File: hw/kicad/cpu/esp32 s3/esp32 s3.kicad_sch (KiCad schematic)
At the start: 42 parts, among them J1 TOP, J2 BUTTOM, J3 USB_B_Micro, SW1 SW_Push, U1 ESP32-S3-WROOM-1-N16R2, U2 ICM-42688-P

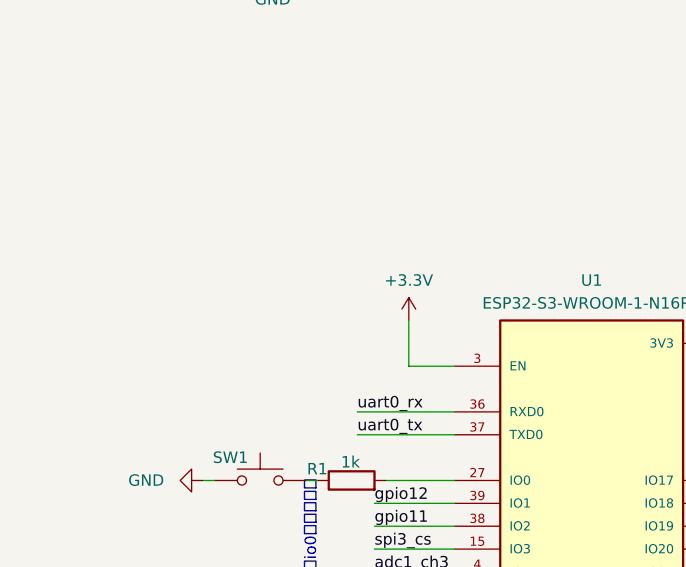
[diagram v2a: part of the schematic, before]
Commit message: 更新ESP32 S3 CPU板
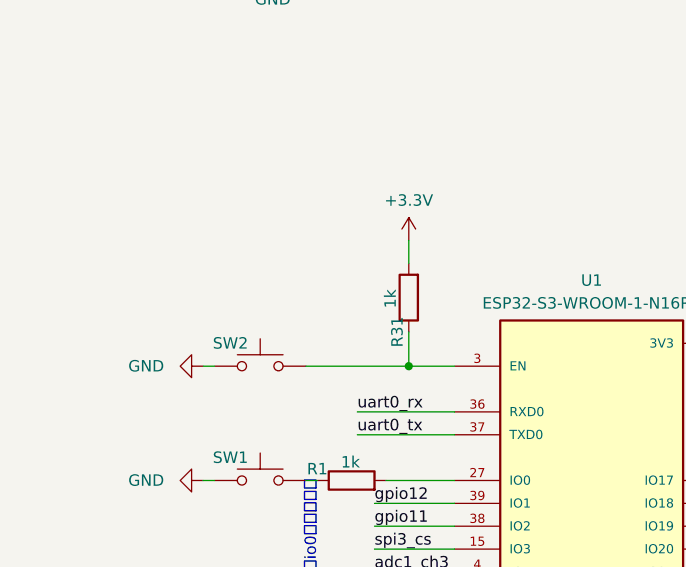
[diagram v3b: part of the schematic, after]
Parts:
- added R31: 1k, Resistor_SMD:R_0603_1608Metric, symbol Device:R
- added SW2: SW_Push, Button_Switch_THT:SW_SPST_Omron_B3F-315x_Angled, symbol Switch:SW_Push
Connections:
- net +3.3V: now also R31.2; no longer U1.3 (EN)
- net GND: now also SW2.1
- new net: R31.1, SW2.2, U1.3 (EN)
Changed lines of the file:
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@@
   (junction (at 263.144 135.382) (diameter 0) (color 0 0 0 0)
+  )
+  (junction (at 67.31 109.22) (diameter 0) (color 0 0 0 0)
   )
   (junction (at 52.197 49.403) (diameter 0) (color 0 0 0 0)
@@
     (stroke (width 0) (type default))
   )
+  (wire (pts (xy 67.31 105.41) (xy 67.31 109.22))
+    (stroke (width 0) (type default))
+  )
   (wire (pts (xy 149.86 80.01) (xy 163.83 80.01))
     (stroke (width 0) (type default))
@@
     (stroke (width 0) (type default))
   )
+  (wire (pts (xy 55.88 109.22) (xy 67.31 109.22))
+    (stroke (width 0) (type default))
+  )
   (wire (pts (xy 245.11 64.77) (xy 254 64.77))
     (stroke (width 0) (type default))
@@
     (stroke (width 0) (type default))
   )
+  (wire (pts (xy 44.45 109.22) (xy 45.72 109.22))
+    (stroke (width 0) (type default))
+  )
   (wire (pts (xy 208.28 64.77) (xy 217.17 64.77))
     (stroke (width 0) (type default))
@@
     (stroke (width 0) (type default))
   )
-  (wire (pts (xy 67.31 104.14) (xy 67.31 109.22))
+  (wire (pts (xy 67.31 95.25) (xy 67.31 97.79))
     (stroke (width 0) (type default))
   )
@@
         (path "/988ee502-8596-4ebe-9b99-0eb76e7d156a"
           (reference "R15") (unit 1)
+        )
+      )
+    )
+  )
+  (symbol (lib_id "Device:R") (at 67.31 101.6 180) (unit 1)
+    (in_bom yes) (on_board yes) (dnp no)
+    (property "Reference" "R31" (at 66.04 105.41 90)
+      (effects (font (size 1.27 1.27)))
+    )
+    (property "Value" "1k" (at 65.278 101.727 90)
+      (effects (font (size 1.27 1.27)))
+    )
+    (property "Footprint" "Resistor_SMD:R_0603_1608Metric" (at 69.088 101.6 90)
+      (effects (font (size 1.27 1.27)) hide)
+    )
+    (property "Datasheet" "~" (at 67.31 101.6 0)
+      (effects (font (size 1.27 1.27)) hide)
+    )
+    (pin "1")
+    (pin "2")
+    (instances
+      (project "esp32 s3"
+        (path "/988ee502-8596-4ebe-9b99-0eb76e7d156a"
+          (reference "R31") (unit 1)
         )
       )
@@
     )
   )
+  (symbol (lib_id "power:GND") (at 44.45 109.22 270) (unit 1)
+    (in_bom yes) (on_board yes) (dnp no) (fields_autoplaced)
+    (property "Reference" "#PWR012" (at 38.1 109.22 0)
+      (effects (font (size 1.27 1.27)) hide)
+    )
+    (property "Value" "GND" (at 40.132 109.22 90)
+      (effects (font (size 1.27 1.27)) (justify right))
+    )
+    (property "Footprint" "" (at 44.45 109.22 0)
+      (effects (font (size 1.27 1.27)) hide)
+    )
+    (property "Datasheet" "" (at 44.45 109.22 0)
+      (effects (font (size 1.27 1.27)) hide)
+    )
+    (pin "1")
+    (instances
+      (project "esp32 s3"
+        (path "/988ee502-8596-4ebe-9b99-0eb76e7d156a"
+          (reference "#PWR012") (unit 1)
+        )
+      )
+    )
+  )
   (symbol (lib_id "Device:R") (at 119.507 58.42 90) (unit 1)
     (in_bom yes) (on_board yes) (dnp no)
@@
     )
   )
-  (symbol (lib_id "power:+3.3V") (at 67.31 104.14 0) (unit 1)
-    (in_bom yes) (on_board yes) (dnp no) (fields_autoplaced)
-    (property "Reference" "#PWR04" (at 67.31 107.95 0)
-      (effects (font (size 1.27 1.27)) hide)
-    )
-    (property "Value" "+3.3V" (at 67.31 99.695 0)
-      (effects (font (size 1.27 1.27)))
-    )
-    (property "Footprint" "" (at 67.31 104.14 0)
-      (effects (font (size 1.27 1.27)) hide)
-    )
-    (property "Datasheet" "" (at 67.31 104.14 0)
+  (symbol (lib_id "power:+3.3V") (at 67.31 95.25 0) (unit 1)
+    (in_bom yes) (on_board yes) (dnp no) (fields_autoplaced)
+    (property "Reference" "#PWR04" (at 67.31 99.06 0)
+      (effects (font (size 1.27 1.27)) hide)
+    )
+    (property "Value" "+3.3V" (at 67.31 90.805 0)
+      (effects (font (size 1.27 1.27)))
+    )
+    (property "Footprint" "" (at 67.31 95.25 0)
+      (effects (font (size 1.27 1.27)) hide)
+    )
+    (property "Datasheet" "" (at 67.31 95.25 0)
       (effects (font (size 1.27 1.27)) hide)
     )
@@
         )
       )
+    )
+  )
+  (symbol (lib_id "Switch:SW_Push") (at 50.8 109.22 0) (unit 1)
+    (in_bom yes) (on_board yes) (dnp no)
+    (property "Reference" "SW2" (at 47.498 106.68 0)
+      (effects (font (size 1.27 1.27)))
+    )
+    (property "Value" "SW_Push" (at 50.8 104.14 0)
+      (effects (font (size 1.27 1.27)) hide)
+    )
+    (property "Footprint" "Button_Switch_THT:SW_SPST_Omron_B3F-315x_Angled" (at 50.8 104.14 0)
+      (effects (font (size 1.27 1.27)) hide)
+    )
+    (property "Datasheet" "~" (at 50.8 104.14 0)
+      (effects (font (size 1.27 1.27)) hide)
+    )
+    (pin "1")
+    (pin "2")
+    (instances
+      (project "esp32 s3"
+        (path "/988ee502-8596-4ebe-9b99-0eb76e7d156a"
+          (reference "SW2") (unit 1)
+        )
+      )

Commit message: 更新USB micro 为优信的封装
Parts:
- J3: footprint Connector_USB:USB_Micro-B_Wuerth_629105150521 -> USB_Micro-B_YouCee:USB_Micro-B_YouCee
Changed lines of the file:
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@@
       (effects (font (size 1.27 1.27)))
     )
-    (property "Footprint" "Connector_USB:USB_Micro-B_Wuerth_629105150521" (at 158.75 136.398 0)
+    (property "Footprint" "USB_Micro-B_YouCee:USB_Micro-B_YouCee" (at 158.75 136.398 0)
       (effects (font (size 1.27 1.27)) hide)
     )
